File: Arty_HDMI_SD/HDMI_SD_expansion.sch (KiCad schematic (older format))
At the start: 54 parts, among them J1 0015912120, J2 1140084168, J3 0015912120, J4 2000-1-2-41-00-BK, J5 UE27AC54100, J6 0015912120, U1 TPS61232DRCT, U2 MAX3421EEHJ, Y1 KX-7_12,MHz

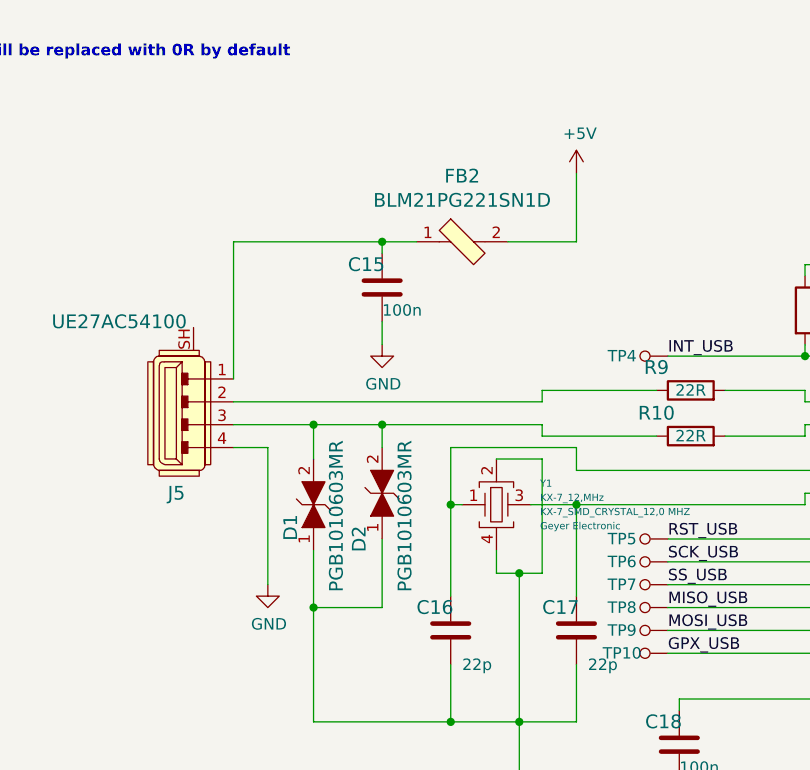
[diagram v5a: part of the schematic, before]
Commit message: Optimized component placement
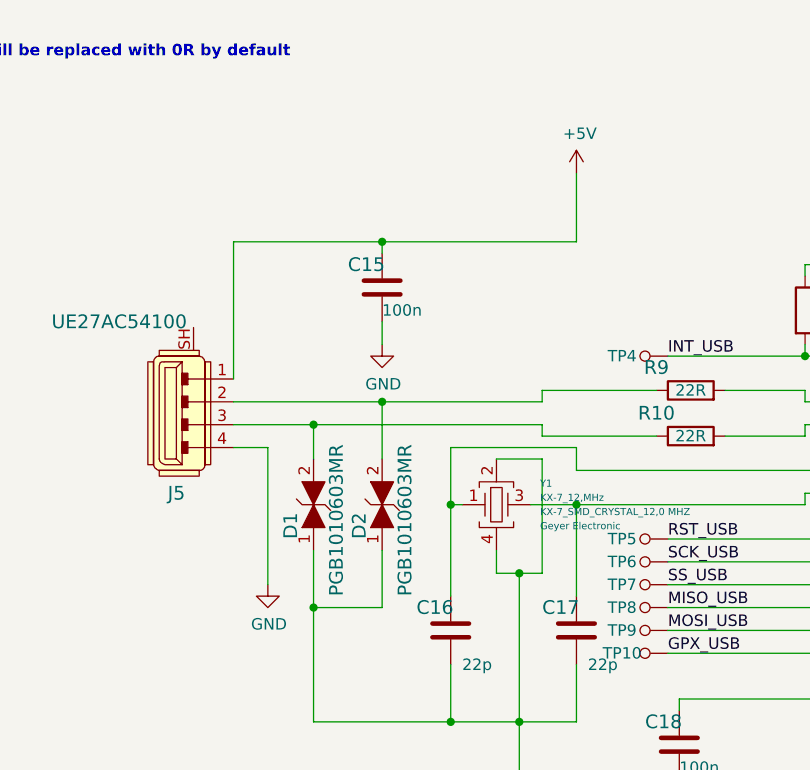
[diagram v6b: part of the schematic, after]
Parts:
- removed FB2: BLM21PG221SN1D, antmicro-footprints:0805, symbol antmicro_Ferrite_Beads_and_Chips:BLM21PG221SN1D
- D1, D2: footprint antmicro-footprints:0603 -> antmicro-footprints:PGB1010603MR
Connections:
- net +5V: now also C15.1, J5.1
- net at J5.2, R9.1: now also D2.2
- net at D1.2, J5.3, R10.1: no longer D2.2
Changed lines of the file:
@@
 	7650 4600 7650 4550
 Wire Wire Line
-	6300 4450 7650 4450
+	6300 4450 6950 4450
 Wire Wire Line
 	6300 4550 6650 4550
@@
 	1    0    0    -1
 $EndComp
-$Comp
-L antmicro_TVS_Diodes:PGB1010603MR D1
-U 1 1 5D80FC7F
-P 6650 4900
-F 0 "D1" H 6550 5000 60  0000 C CNN
-F 1 "PGB1010603MR" H 6600 4800 60  0000 C CNN
-F 2 "antmicro-footprints:0603" H 6850 5100 60  0001 L CNN
-F 3 "https://www.littelfuse.com/data/en/data_sheets/littelfuse_pulseguard-esd_pgb1.pdf" H 6850 5200 60  0001 L CNN
-F 4 "Littelfuse Inc." H 6850 6000 60  0001 L CNN "Manufacturer"
-F 5 "PGB1010603MR" H 6850 5400 60  0001 L CNN "MPN"
-	1    6650 4900
-	0    -1   -1   0
-$EndComp
-$Comp
-L antmicro_TVS_Diodes:PGB1010603MR D2
-U 1 1 5D80FCE5
-P 6950 4850
-F 0 "D2" H 6750 4950 60  0000 C CNN
-F 1 "PGB1010603MR" H 6850 4750 60  0000 C CNN
-F 2 "antmicro-footprints:0603" H 7150 5050 60  0001 L CNN
-F 3 "https://www.littelfuse.com/data/en/data_sheets/littelfuse_pulseguard-esd_pgb1.pdf" H 7150 5150 60  0001 L CNN
-F 4 "Littelfuse Inc." H 7150 5950 60  0001 L CNN "Manufacturer"
-F 5 "PGB1010603MR" H 7150 5350 60  0001 L CNN "MPN"
-	1    6950 4850
-	0    -1   -1   0
-$EndComp
 Wire Wire Line
 	6650 4550 6650 4700
 Connection ~ 6650 4550
-Wire Wire Line
-	6650 4550 6950 4550
-Wire Wire Line
-	6950 4650 6950 4550
-Connection ~ 6950 4550
-Wire Wire Line
-	6950 4550 7650 4550
+Connection ~ 6950 4450
 Wire Wire Line
 	6650 5100 6650 5350
@@
 	6650 5350 6950 5350
 Wire Wire Line
-	6950 5350 6950 5050
+	6950 5350 6950 5100
 Wire Wire Line
 	6650 5350 6650 5850
@@
 	1    0    0    -1
 $EndComp
-$Comp
-L antmicro_Ferrite_Beads_and_Chips:BLM21PG221SN1D FB2
-U 1 1 5DBC677D
-P 7300 3750
-F 0 "FB2" H 7300 4037 60  0000 C CNN
-F 1 "BLM21PG221SN1D" H 7300 3931 60  0000 C CNN
-F 2 "antmicro-footprints:0805" H 7500 3950 60  0001 L CNN
-F 3 "https://www.murata.com/en-us/products/en-us/products/productdata/8796738977822/ENFA0005.pdf" H 7500 4050 60  0001 L CNN
-F 4 "BLM21PG221SN1D" H 7500 4250 60  0001 L CNN "MPN"
-F 5 "Murata Electronics North America" H 7500 4850 60  0001 L CNN "Manufacturer"
-	1    7300 3750
-	1    0    0    -1
-$EndComp
 Wire Wire Line
 	6300 4350 6300 3750
@@
 $EndComp
 Wire Wire Line
-	7500 3750 7800 3750
-Wire Wire Line
 	7800 3750 7800 3450
 Wire Wire Line
 	6950 3800 6950 3750
 Connection ~ 6950 3750
-Wire Wire Line
-	6950 3750 7100 3750
 $Comp
 L power:GND #PWR0118
@@
 RST_USB
 Wire Wire Line
-	6450 4650 6450 5250
-Wire Wire Line
 	8800 4250 8200 4250
 Connection ~ 8800 4250
@@
 	0    1    1    0
 $EndComp
+$Comp
+L antmicro_TVS_Diodes:PGB1010603MR D1
+U 1 1 5D78B2C1
+P 6650 4900
+F 0 "D1" H 6500 5000 60  0000 L CNN
+F 1 "PGB1010603MR" H 6250 4800 60  0000 L CNN
+F 2 "antmicro-footprints:PGB1010603MR" H 6850 5100 60  0001 L CNN
+F 3 "https://www.littelfuse.com/data/en/data_sheets/littelfuse_pulseguard-esd_pgb1.pdf" H 6850 5200 60  0001 L CNN
+F 4 "Littelfuse Inc." H 6850 6000 60  0001 L CNN "Manufacturer"
+F 5 "PGB1010603MR" H 6850 5400 60  0001 L CNN "MPN"
+	1    6650 4900
+	0    -1   -1   0
+$EndComp
+Wire Wire Line
+	6450 4650 6450 5250
+$Comp
+L antmicro_TVS_Diodes:PGB1010603MR D2
+U 1 1 5D7BDFD2
+P 6950 4900
+F 0 "D2" H 6800 5000 60  0000 L CNN
+F 1 "PGB1010603MR" H 6550 4800 60  0000 L CNN
+F 2 "antmicro-footprints:PGB1010603MR" H 7150 5100 60  0001 L CNN
+F 3 "https://www.littelfuse.com/data/en/data_sheets/littelfuse_pulseguard-esd_pgb1.pdf" H 7150 5200 60  0001 L CNN
+F 4 "Littelfuse Inc." H 7150 6000 60  0001 L CNN "Manufacturer"
+F 5 "PGB1010603MR" H 7150 5400 60  0001 L CNN "MPN"
+	1    6950 4900
+	0    -1   -1   0
+$EndComp
+Wire Wire Line
+	6950 3750 7800 3750
+Wire Wire Line
+	6950 4700 6950 4550
+Wire Wire Line
+	6950 4450 7650 4450
+Wire Wire Line
+	6950 4550 6950 4450
+Wire Wire Line
+	6650 4550 7650 4550
 $EndSCHEMATC

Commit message: PCB routing
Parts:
- added N1: antmicro_logo, antmicro-footprints:antmicro-logo_scaled_30mm, symbol antmicro_Mechanical_Parts:antmicro_logo
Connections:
- net TDMS_CLK_N: now also J3.10; no longer J3.4
- net TDMS_CLK_P: now also J3.9; no longer J3.3
- net TDMS_D0_N: now also J3.2; no longer J3.8
- net TDMS_D0_P: now also J3.1; no longer J3.7
- net TDMS_D1_N: now also J3.4; no longer J3.10
- net TDMS_D1_P: now also J3.3; no longer J3.9
- net TDMS_D2_N: now also J3.8; no longer J3.2
- net TDMS_D2_P: now also J3.7; no longer J3.1
- net D-: now reaches R9.2, U2.20 (D-)
- net D+: now reaches R10.2, U2.21 (D+)
- net Data+: now reaches D1.2, J5.3, R10.1
- net Data-: now reaches D2.2, J5.2, R9.1
- removed net NC: J4.13, J4.14, J4.15, J4.16, J4.18, J4.19
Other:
- note removed: "?"
- moved on the sheet: J4
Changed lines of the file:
@@
 $EndDescr
 Wire Wire Line
-	9300 1250 8750 1250
-Wire Wire Line
-	9300 1350 8750 1350
-Wire Wire Line
-	10100 1450 10700 1450
-Wire Wire Line
-	9300 1550 8750 1550
-Wire Wire Line
-	10100 1850 10700 1850
-Wire Wire Line
-	10100 1350 10700 1350
-Wire Wire Line
-	9300 1850 8750 1850
-Wire Wire Line
-	9300 1950 8750 1950
-Wire Wire Line
-	10100 2050 10700 2050
-Wire Wire Line
-	10700 1950 10100 1950
-Text Label 8750 1250 0    50   ~ 0
+	9050 1500 8500 1500
+Wire Wire Line
+	9050 1600 8500 1600
+Wire Wire Line
+	9850 1700 10450 1700
+Wire Wire Line
+	9050 1800 8500 1800
+Wire Wire Line
+	9850 2100 10450 2100
+Wire Wire Line
+	9850 1600 10450 1600
+Text Label 8500 1500 0    50   ~ 0
 C_TDMS_D2_P
-Text Label 8750 1350 0    50   ~ 0
+Text Label 8500 1600 0    50   ~ 0
 C_TDMS_D2_N
-Text Label 10700 1450 2    50   ~ 0
+Text Label 10450 1700 2    50   ~ 0
 C_TDMS_D1_P
 Wire Wire Line
-	10100 1550 10700 1550
-Text Label 10700 1550 2    50   ~ 0
+	9850 1800 10450 1800
+Text Label 10450 1800 2    50   ~ 0
 C_TDMS_D1_N
-Text Label 8750 1550 0    50   ~ 0
+Text Label 8500 1800 0    50   ~ 0
 C_TDMS_D0_P
-Text Label 8750 1650 0    50   ~ 0
+Text Label 8500 1900 0    50   ~ 0
 C_TDMS_D0_N
-Text Label 10700 1750 2    50   ~ 0
+Text Label 10450 2000 2    50   ~ 0
 C_TDMS_CLK_P
-Text Label 10700 1850 2    50   ~ 0
+Text Label 10450 2100 2    50   ~ 0
 C_TDMS_CLK_N
-Text Label 10700 1350 2    50   ~ 0
+Text Label 10450 1600 2    50   ~ 0
 GND
-Text Label 8750 1850 0    50   ~ 0
-NC
-Text Label 8750 1950 0    50   ~ 0
-NC
 $Comp
 L power:GND #PWR0101
 U 1 1 5D608454
-P 9400 2800
-F 0 "#PWR0101" H 9400 2550 50  0001 C CNN
-F 1 "GND" H 9405 2627 50  0000 C CNN
-F 2 "" H 9400 2800 50  0001 C CNN
-F 3 "" H 9400 2800 50  0001 C CNN
-	1    9400 2800
-	1    0    0    -1
-$EndComp
-Text Label 10700 2050 2    50   ~ 0
-NC
-Text Label 10700 1950 2    50   ~ 0
-NC
-$Comp
-L antmicro_Rectangular_Connectors_Headers_Male_Pins:0015912120 J3
-U 1 1 5D60CB7D
-P 3950 1300
-F 0 "J3" H 3950 1747 60  0000 C CNN
-F 1 "0015912120" H 3950 1641 60  0000 C CNN
-F 2 "antmicro-footprints:PinHeader_6x2_P2.54mm_Horizontal_Mirrored" H 4150 1500 60  0001 L CNN
-F 3 "https://www.molex.com/pdm_docs/sd/015912120_sd.pdf" H 4150 1600 60  0001 L CNN
-F 4 "0015912120" H 4150 1800 60  0001 L CNN "MPN"
-F 5 "Molex" H 4150 2400 60  0001 L CNN "Manufacturer"
-	1    3950 1300
-	1    0    0    -1
-$EndComp
-Wire Wire Line
-	3750 1100 3200 1100
-Wire Wire Line
-	3750 1200 3200 1200
+P 9150 3050
+F 0 "#PWR0101" H 9150 2800 50  0001 C CNN
+F 1 "GND" H 9155 2877 50  0000 C CNN
+F 2 "" H 9150 3050 50  0001 C CNN
+F 3 "" H 9150 3050 50  0001 C CNN
+	1    9150 3050
+	1    0    0    -1
+$EndComp
+Wire Wire Line
+	4150 1100 4700 1100
+Wire Wire Line
+	4150 1200 4700 1200
+Wire Wire Line
+	4150 1300 4700 1300
+Text Label 4700 1100 2    50   ~ 0
+TDMS_D2_P
+Text Label 4700 1200 2    50   ~ 0
+TDMS_D2_N
+Text Label 4700 1300 2    50   ~ 0
+TDMS_CLK_P
+Wire Wire Line
+	4150 1400 4700 1400
+Text Label 4700 1400 2    50   ~ 0
+TDMS_CLK_N
 Wire Wire Line
 	3750 1300 3200 1300
-Text Label 3200 1100 0    50   ~ 0
-TDMS_D2_P
-Text Label 3200 1200 0    50   ~ 0
-TDMS_D2_N
 Text Label 3200 1300 0    50   ~ 0
-TDMS_CLK_P
+TDMS_D1_P
 Wire Wire Line
 	3750 1400 3200 1400
 Text Label 3200 1400 0    50   ~ 0
-TDMS_CLK_N
-Wire Wire Line
-	4150 1300 4700 1300
-Text Label 4700 1300 2    50   ~ 0
-TDMS_D1_P
-Wire Wire Line
-	4150 1400 4700 1400
-Text Label 4700 1400 2    50   ~ 0
 TDMS_D1_N
 Wire Wire Line
-	4150 1100 4700 1100
-Wire Wire Line
-	4150 1200 4700 1200
-Text Label 4700 1100 2    50   ~ 0
+	3750 1100 3200 1100
+Wire Wire Line
+	3750 1200 3200 1200
+Text Label 3200 1100 0    50   ~ 0
 TDMS_D0_P
-Text Label 4700 1200 2    50   ~ 0
+Text Label 3200 1200 0    50   ~ 0
 TDMS_D0_N
 Wire Wire Line
@@
 Text Label 3200 1600 0    50   ~ 0
 +3V3
-$Comp
-L antmicro_Rectangular_Connectors_Headers_Male_Pins:0015912120 J1
-U 1 1 5D618F18
-P 1550 1300
-F 0 "J1" H 1550 1747 60  0000 C CNN
-F 1 "0015912120" H 1550 1641 60  0000 C CNN
-F 2 "antmicro-footprints:PinHeader_6x2_P2.54mm_Horizontal_Mirrored" H 1750 1500 60  0001 L CNN
-F 3 "https://www.molex.com/pdm_docs/sd/015912120_sd.pdf" H 1750 1600 60  0001 L CNN
-F 4 "0015912120" H 1750 1800 60  0001 L CNN "MPN"
-F 5 "Molex" H 1750 2400 60  0001 L CNN "Manufacturer"
-	1    1550 1300
-	1    0    0    -1
-$EndComp
 Wire Wire Line
 	1350 1100 800  1100
@@
 L antmicro_USB_DVI_HDMI_Connectors:2000-1-2-41-00-BK J4
 U 1 1 5D6CFFFB
-P 9700 1750
-F 0 "J4" H 9700 2687 60  0000 C CNN
-F 1 "2000-1-2-41-00-BK" H 9700 2581 60  0000 C CNN
-F 2 "antmicro-footprints:HDMI_A_Female_2000-1-2-41-00-BK" H 9900 1950 60  0001 L CNN
-F 3 "http://www.cnctech.us/pdfs/2000-1-2-41-00-BK.pdf" H 9900 2050 60  0001 L CNN
-F 4 "2000-1-2-41-00-BK" H 9900 2250 60  0001 L CNN "MPN"
-F 5 "CNC Tech" H 9900 2850 60  0001 L CNN "Manufacturer"
-	1    9700 1750
-	1    0    0    -1
-$EndComp
-Wire Wire Line
-	8750 1650 9300 1650
-Wire Wire Line
-	9300 1450 8750 1450
-Text Label 8750 1450 0    50   ~ 0
+P 9450 2000
+F 0 "J4" H 9450 2937 60  0000 C CNN
+F 1 "2000-1-2-41-00-BK" H 9450 2831 60  0000 C CNN
+F 2 "antmicro-footprints:HDMI_A_Female_2000-1-2-41-00-BK" H 9650 2200 60  0001 L CNN
+F 3 "http://www.cnctech.us/pdfs/2000-1-2-41-00-BK.pdf" H 9650 2300 60  0001 L CNN
+F 4 "2000-1-2-41-00-BK" H 9650 2500 60  0001 L CNN "MPN"
+F 5 "CNC Tech" H 9650 3100 60  0001 L CNN "Manufacturer"
+	1    9450 2000
+	1    0    0    -1
+$EndComp
+Wire Wire Line
+	8500 1900 9050 1900
+Wire Wire Line
+	9050 1700 8500 1700
+Text Label 8500 1700 0    50   ~ 0
 GND
 Wire Wire Line
-	10700 1750 10100 1750
-Wire Wire Line
-	10100 1650 10700 1650
-Text Label 10700 1650 2    50   ~ 0
+	10450 2000 9850 2000
+Wire Wire Line
+	9850 1900 10450 1900
+Text Label 10450 1900 2    50   ~ 0
 GND
 Wire Wire Line
-	9300 1750 8750 1750
-Text Label 8750 1750 0    50   ~ 0
+	9050 2000 8500 2000
+Text Label 8500 2000 0    50   ~ 0
 GND
 Wire Wire Line
-	9400 2550 9400 2800
-Wire Wire Line
-	9300 2050 8750 2050
-Text Label 8750 2050 0    50   ~ 0
+	9150 2800 9150 3050
+Wire Wire Line
+	9050 2300 8500 2300
+Text Label 8500 2300 0    50   ~ 0
 GND
-Wire Wire Line
-	9300 2150 8750 2150
-Text Label 8750 2150 0    50   ~ 0
-NC
 Text Notes 600  750  0    98   ~ 0
 SD_CON_#1
 Text Notes 2900 750  0    98   ~ 0
 HDMI_CON_#2
-Text Notes 8500 750  0    98   ~ 0
+Text Notes 8350 900  0    98   ~ 0
 HDMI_INTERFACE
 Text Notes 650  4800 0    98   ~ 0
@@
 	1    0    0    -1
 $EndComp
-Wire Wire Line
-	10100 2150 10700 2150
-Text Label 10700 2150 2    50   ~ 0
-NC
 Wire Wire Line
 	3600 6400 3900 6400
@@
 Wire Wire Line
 	6000 2300 6000 2400
-$Comp
-L antmicro_Rectangular_Connectors_Headers_Male_Pins:0015912120 J6
-U 1 1 5DC8649C
-P 1600 2600
-F 0 "J6" H 1600 3047 60  0000 C CNN
-F 1 "0015912120" H 1600 2941 60  0000 C CNN
-F 2 "antmicro-footprints:PinHeader_6x2_P2.54mm_Horizontal_Mirrored" H 1800 2800 60  0001 L CNN
-F 3 "https://www.molex.com/pdm_docs/sd/015912120_sd.pdf" H 1800 2900 60  0001 L CNN
-F 4 "0015912120" H 1800 3100 60  0001 L CNN "MPN"
-F 5 "Molex" H 1800 3700 60  0001 L CNN "Manufacturer"
-	1    1600 2600
-	1    0    0    -1
-$EndComp
 Wire Wire Line
 	1400 2400 850  2400
@@
 Text Notes 600  2000 0    98   ~ 0
 USB_CON_#3
-Text Notes 5100 500  0    197  ~ 0
-?
 Text Notes 5550 800  0    118  ~ 0
 DC-DC Step UP
@@
 Text Label 2000 2400 0    50   ~ 0
 GPX_USB
-Text Label 2000 2500 0    50   ~ 0
-RST_USB
 Wire Wire Line
 	8800 4250 8200 4250
@@
 Wire Wire Line
 	6650 4550 7650 4550
+Text Label 2000 2500 0    50   ~ 0
+RST_USB
+$Comp
+L antmicro_Rectangular_Connectors_Headers_Male_Pins:0015912120 J3
+U 1 1 5D60CB7D
+P 3950 1300
+F 0 "J3" H 3950 1747 60  0000 C CNN
+F 1 "0015912120" H 3950 1641 60  0000 C CNN
+F 2 "antmicro-footprints:PinHeader_6x2_P2.54mm_Horizontal_Mirrored" H 4150 1500 60  0001 L CNN
+F 3 "https://www.molex.com/pdm_docs/sd/015912120_sd.pdf" H 4150 1600 60  0001 L CNN
+F 4 "0015912120" H 4150 1800 60  0001 L CNN "MPN"
+F 5 "Molex" H 4150 2400 60  0001 L CNN "Manufacturer"
+	1    3950 1300
+	1    0    0    -1
+$EndComp
+$Comp
+L antmicro_Rectangular_Connectors_Headers_Male_Pins:0015912120 J6
+U 1 1 5DC8649C
+P 1600 2600
+F 0 "J6" H 1600 3047 60  0000 C CNN
+F 1 "0015912120" H 1600 2941 60  0000 C CNN
+F 2 "antmicro-footprints:PinHeader_6x2_P2.54mm_Horizontal_Mirrored" H 1800 2800 60  0001 L CNN
+F 3 "https://www.molex.com/pdm_docs/sd/015912120_sd.pdf" H 1800 2900 60  0001 L CNN
+F 4 "0015912120" H 1800 3100 60  0001 L CNN "MPN"
+F 5 "Molex" H 1800 3700 60  0001 L CNN "Manufacturer"
+	1    1600 2600
+	1    0    0    -1
+$EndComp
+$Comp
+L antmicro_Rectangular_Connectors_Headers_Male_Pins:0015912120 J1
+U 1 1 5D618F18
+P 1550 1300
+F 0 "J1" H 1550 1747 60  0000 C CNN
+F 1 "0015912120" H 1550 1641 60  0000 C CNN
+F 2 "antmicro-footprints:PinHeader_6x2_P2.54mm_Horizontal_Mirrored" H 1750 1500 60  0001 L CNN
+F 3 "https://www.molex.com/pdm_docs/sd/015912120_sd.pdf" H 1750 1600 60  0001 L CNN
+F 4 "0015912120" H 1750 1800 60  0001 L CNN "MPN"
+F 5 "Molex" H 1750 2400 60  0001 L CNN "Manufacturer"
+	1    1550 1300
+	1    0    0    -1
+$EndComp
+Text Label 8600 4600 0    50   ~ 0
+D+
+Text Label 8600 4400 0    50   ~ 0
+D-
+Text Label 7300 4450 0    50   ~ 0
+Data-
+Text Label 7300 4550 0    50   ~ 0
+Data+
+$Comp
+L antmicro_Mechanical_Parts:antmicro_logo N1
+U 1 1 5D84596D
+P 10450 750
+F 0 "N1" H 10850 600 50  0000 C CNN
+F 1 "antmicro_logo" H 10500 600 50  0000 C CNN
+F 2 "antmicro-footprints:antmicro-logo_scaled_30mm" H 10350 1000 50  0001 C CNN
+F 3 "" H 10450 1100 50  0001 C CNN
+	1    10450 750
+	1    0    0    -1
+$EndComp
 $EndSCHEMATC

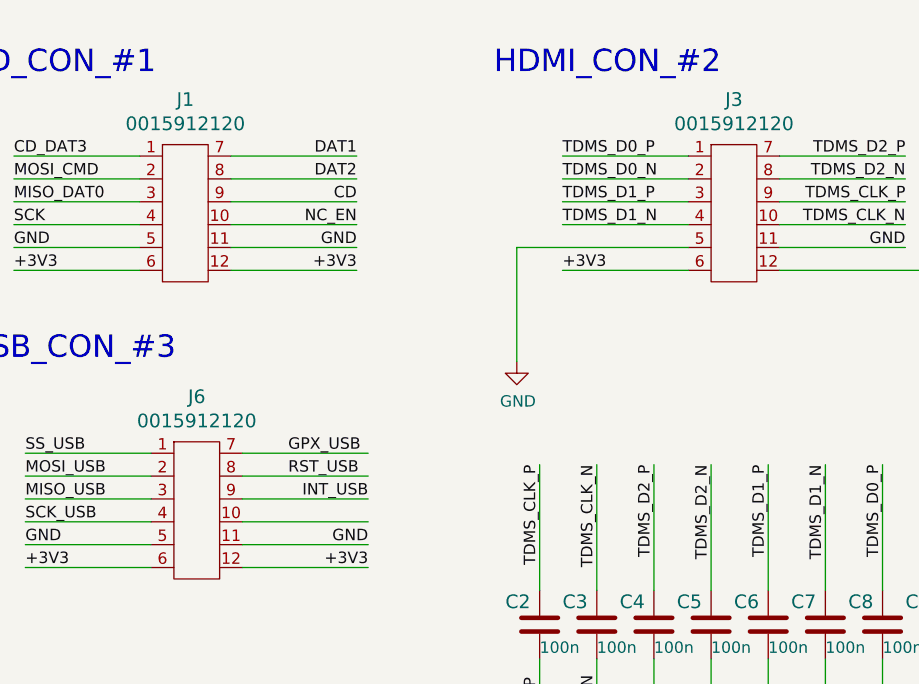
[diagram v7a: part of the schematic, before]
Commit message: Updated PMOD connectors on PCB
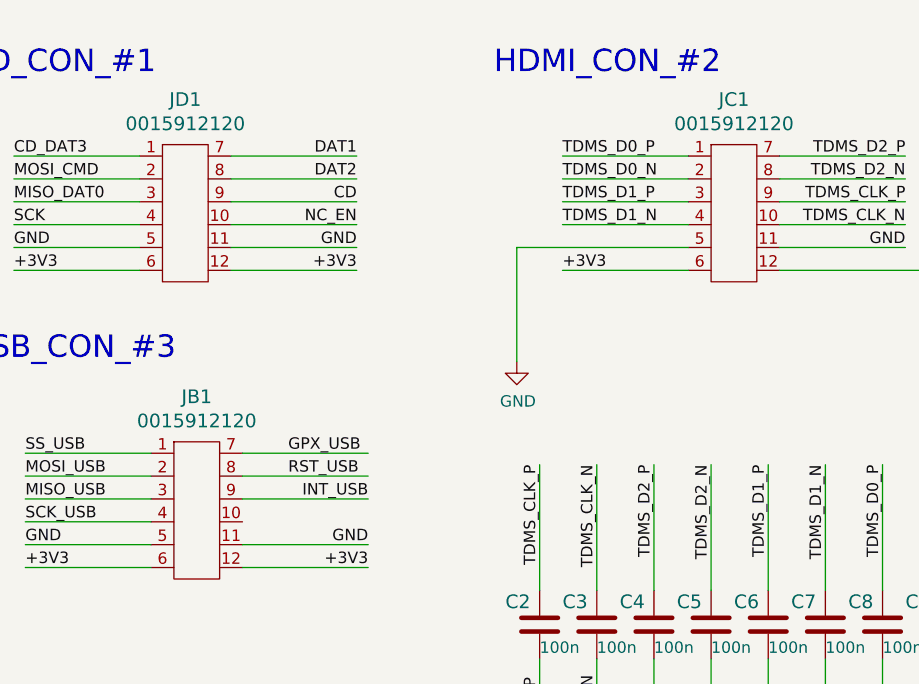
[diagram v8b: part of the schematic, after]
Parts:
- renumbered J6 to JB1, J3 to JC1, J1 to JD1
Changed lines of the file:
@@
 	1800 2600 2350 2600
-Wire Wire Line
-	2350 2700 1800 2700
 Wire Wire Line
 	850  2800 1400 2800
@@
 RST_USB
 $Comp
-L antmicro_Rectangular_Connectors_Headers_Male_Pins:0015912120 J3
+L antmicro_Rectangular_Connectors_Headers_Male_Pins:0015912120 JC1
 U 1 1 5D60CB7D
 P 3950 1300
-F 0 "J3" H 3950 1747 60  0000 C CNN
+F 0 "JC1" H 3950 1747 60  0000 C CNN
 F 1 "0015912120" H 3950 1641 60  0000 C CNN
 F 2 "antmicro-footprints:PinHeader_6x2_P2.54mm_Horizontal_Mirrored" H 4150 1500 60  0001 L CNN
@@
 $EndComp
 $Comp
-L antmicro_Rectangular_Connectors_Headers_Male_Pins:0015912120 J6
+L antmicro_Rectangular_Connectors_Headers_Male_Pins:0015912120 JB1
 U 1 1 5DC8649C
 P 1600 2600
-F 0 "J6" H 1600 3047 60  0000 C CNN
+F 0 "JB1" H 1600 3047 60  0000 C CNN
 F 1 "0015912120" H 1600 2941 60  0000 C CNN
 F 2 "antmicro-footprints:PinHeader_6x2_P2.54mm_Horizontal_Mirrored" H 1800 2800 60  0001 L CNN
@@
 $EndComp
 $Comp
-L antmicro_Rectangular_Connectors_Headers_Male_Pins:0015912120 J1
+L antmicro_Rectangular_Connectors_Headers_Male_Pins:0015912120 JD1
 U 1 1 5D618F18
 P 1550 1300
-F 0 "J1" H 1550 1747 60  0000 C CNN
+F 0 "JD1" H 1550 1747 60  0000 C CNN
 F 1 "0015912120" H 1550 1641 60  0000 C CNN
 F 2 "antmicro-footprints:PinHeader_6x2_P2.54mm_Horizontal_Mirrored" H 1750 1500 60  0001 L CNN
